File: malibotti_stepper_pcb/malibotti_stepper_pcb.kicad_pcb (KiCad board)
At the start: 2 copper layers, 80 x 65 mm, 40 parts, among them J1 Stepper 1, J5 USB_C_Receptacle_USB2.0_16P, J6 Conn_01x04, SW1 RST, SW8 BTN, U1 ESP32-C3-MINI-1, U2 XC6206PxxxMR, U3 STSPIN220

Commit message: Malibotti WIP
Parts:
- removed TP2: M1_1, TestPoint:TestPoint_Pad_1.5x1.5mm
- added C13: 1n, Capacitor_SMD:C_0402_1005Metric, B.Cu at (85.3, 105.7)
- added C14: 1n, Capacitor_SMD:C_0402_1005Metric, B.Cu at (85.5, 108.7)
- added C15: u1, Capacitor_SMD:C_0402_1005Metric, B.Cu at (89.3, 109.6)
- added C16: 22n, Capacitor_SMD:C_0402_1005Metric, B.Cu at (87.4, 110.5)
- added C17: 22u, Capacitor_SMD:C_0603_1608Metric, B.Cu at (92.0, 93.8)
- added C18: 2u2, Capacitor_SMD:C_0603_1608Metric, B.Cu at (92.0, 95.2)
- added J2: Stepper 1, liebler_CONN:JST_XH_5P_SMD, B.Cu at (100.2, 104.8)
- added J3: Servo, Connector_PinHeader_2.54mm:PinHeader_1x03_P2.54mm_Vertical, B.Cu at (134.4, 118.2)
- added J4: Conn_01x04, liebler_CONN:JST_XH_S4B-XH-A-1_1x04_P2.50mm_Horizontal_SmallerCourtyard, F.Cu at (104.8, 75.2)
- added R15: 1k, Resistor_SMD:R_0402_1005Metric, B.Cu at (85.3, 106.7)
- added R16: 1k, Resistor_SMD:R_0402_1005Metric, B.Cu at (84.5, 108.7)
- added R17: 1k, Resistor_SMD:R_0402_1005Metric, B.Cu at (90.2, 110.2)
- added R18: 1k, Resistor_SMD:R_0402_1005Metric, B.Cu at (87.4, 108.7)
- added R19: 10k, Resistor_SMD:R_0402_1005Metric, B.Cu at (86.5, 108.7)
- added R20: 1r0, Resistor_SMD:R_0805_2012Metric_Pad1.20x1.40mm_HandSolder, B.Cu at (92.0, 101.8)
- added R21: 1r0, Resistor_SMD:R_0805_2012Metric_Pad1.20x1.40mm_HandSolder, B.Cu at (92.0, 109.0)
- added R22: 10k, Resistor_SMD:R_0402_1005Metric, B.Cu at (95.3, 90.9)
- added R23: 10k, Resistor_SMD:R_0402_1005Metric, B.Cu at (88.3, 108.7)
- added R24: 5k1, Resistor_SMD:R_0402_1005Metric, B.Cu at (95.3, 89.0)
- added R25: 5k1, Resistor_SMD:R_0402_1005Metric, B.Cu at (88.3, 110.5)
- added R5: 1r0, Resistor_SMD:R_0805_2012Metric_Pad1.20x1.40mm_HandSolder, B.Cu at (92.0, 90.9)
- added R6: 1r0, Resistor_SMD:R_0805_2012Metric_Pad1.20x1.40mm_HandSolder, B.Cu at (92.0, 98.2)
- added U4: STSPIN220, Package_DFN_QFN:VQFN-16-1EP_3x3mm_P0.5mm_EP1.8x1.8mm, B.Cu at (88.5, 105.5)
- C7: footprint Capacitor_SMD:C_0603_1608Metric -> Capacitor_SMD:C_0402_1005Metric
- J1: footprint liebler_CONN:JST_XH_B5B-XH-A_1x05_P2.50mm_Vertical_smaller -> liebler_CONN:JST_XH_5P_SMD
- J6: moved to F.Cu
- R10: value 47k -> 10k
- U3: moved to B.Cu
- moved R9 129.2 mm to (90.7, 77.9), turned to -90 degrees
- moved R8 127.3 mm to (91.8, 77.9), turned to -90 degrees
- moved R1 125.7 mm to (89.8, 77.9), turned to -90 degrees
- moved R7 125.1 mm to (93.2, 77.8), turned to -90 degrees
- moved J6 123.5 mm to (117.5, 75.2)
- moved R4 118.4 mm to (102.3, 73.2), turned to 90 degrees
- moved R12 115.7 mm to (94.3, 89.8), turned to -90 degrees
- moved R3 115.3 mm to (104.8, 73.2), turned to 90 degrees
- moved R11 112.6 mm to (96.4, 90.9), turned to -90 degrees
- moved R14 112.3 mm to (99.2, 90.9), turned to 90 degrees
- moved R13 111.1 mm to (98.8, 92.8), turned to 0 degrees
- moved R10 111.0 mm to (97.3, 90.9), turned to -90 degrees
- moved C3 110.1 mm to (71.2, 115.4)
- moved C2 103.4 mm to (81.2, 90.6)
- moved SW8 102.2 mm to (83.5, 80.0), turned to -90 degrees
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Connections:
- J6 pad 2: BUZZER -> Net-(J6-Pin_2)
- R12 pad 1: PWM -> GND
- TP3 pad 1: /M1_2 -> unconnected-(TP3-Pad1)
- U1 pad 12: /M2_2 -> unconnected-(U1-GPIO0/ADC1_CH0/XTAL_32K_P-Pad12)
- U1 pad 13: /M2_1 -> unconnected-(U1-GPIO1/ADC1_CH1/XTAL_32K_N-Pad13)
- U1 pad 16: /M1_1 -> unconnected-(U1-GPIO10-Pad16)
- U1 pad 18: /M1_2 -> unconnected-(U1-GPIO4/ADC1_CH4-Pad18)
- U1 pad 30: BUZZER -> Net-(J6-Pin_2)
- U1 pad 5: SERVO2_ADC -> STEP2
- U1 pad 6: SERVO1_ADC -> DIR2
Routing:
- net /TX: track 0.00 -> 55.1 mm
- net Net-(J6-Pin_2): track 0.00 -> 52.3 mm
- net /USBD+: track 0.00 -> 47.9 mm
- net /USBD-: track 0.00 -> 47.1 mm
- net Net-(J2-Pin_2): track 0.00 -> 21.2 mm
- net Net-(J1-Pin_2): track 0.00 -> 21.1 mm
- net Net-(J1-Pin_1): track 0.00 -> 9.55 mm
- net Net-(J2-Pin_1): track 0.00 -> 7.46 mm
- net Net-(J1-Pin_3): track 0.00 -> 7.26 mm
- net Net-(J2-Pin_3): track 0.00 -> 7.23 mm
- net Net-(J1-Pin_4): track 0.00 -> 6.99 mm
- net Net-(J2-Pin_4): track 0.00 -> 6.94 mm
- net +3V3: track 0.00 -> 6.03 mm
- net Net-(J5-D--PadA7): track 0.00 -> 4.94 mm
- net Net-(U3-REF): track 0.00 -> 4.36 mm
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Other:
- board size 80 x 65 mm -> 70 x 65 mm

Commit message: WIP
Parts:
- J3: footprint Connector_PinHeader_2.54mm:PinHeader_1x03_P2.54mm_Vertical -> Connector_PinHeader_2.54mm:PinHeader_1x03_P2.54mm_Vertical_SMD_Pin1Left
- moved SW1 102.2 mm to (84.3, 120.8), turned to 90 degrees
- moved BZ1 65.7 mm to (101.1, 81.2), turned to 90 degrees
- moved J3 48.6 mm to (95.6, 88.9), turned to 90 degrees
- moved H1 44.0 mm to (120.5, 93.0)
- moved D21 35.0 mm to (79.8, 100.0), turned to -90 degrees
- moved C3 21.4 mm to (79.8, 95.8)
- moved R2 19.4 mm to (94.9, 84.5)
- moved C1 15.6 mm to (82.3, 73.3)
- moved C2 15.6 mm to (82.5, 75.0)
- moved U2 11.3 mm to (84.5, 77.5)
- moved C4 10.7 mm to (87.8, 78.5)
- moved SW8 6.38 mm to (87.4, 85.0), turned to 90 degrees
- moved C15 4.30 mm to (89.3, 113.9)
- moved J1 4.30 mm to (84.0, 99.2)
- moved J2 4.30 mm to (100.2, 109.2)
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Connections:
- net Net-(J6-Pin_2) renamed /RX
- C13 pad 1: RESET2 -> STEPPER_RESET
- C9 pad 1: RESET1 -> STEPPER_RESET
- R13 pad 1: RESET1 -> STEPPER_RESET
- R15 pad 1: RESET2 -> STEPPER_RESET
- R25 pad 1: +3V3 -> Net-(R23-Pad1)
- R25 pad 2: Net-(R23-Pad1) -> +3V3
- U1 pad 12: unconnected-(U1-GPIO0/ADC1_CH0/XTAL_32K_P-Pad12) -> BUZZER
- U1 pad 13: unconnected-(U1-GPIO1/ADC1_CH1/XTAL_32K_N-Pad13) -> STEPPER_RESET
- U1 pad 16: unconnected-(U1-GPIO10-Pad16) -> STEP1
- U1 pad 18: unconnected-(U1-GPIO4/ADC1_CH4-Pad18) -> DIR1
- U1 pad 19: SRV3 -> Servo1
- U3 pad 14: RESET1 -> STEPPER_RESET
- U4 pad 14: RESET2 -> STEPPER_RESET
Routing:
- net SCL: track 0.00 -> 50.8 mm, vias 0 -> 2
- net SDA: track 0.00 -> 50.0 mm, vias 0 -> 4
- net STEPPER_RESET: track 0.00 -> 46.5 mm, vias 0 -> 4
- net BUZZER: track 0.00 -> 46.4 mm, vias 0 -> 2
- net Servo1: track 0.00 -> 35.7 mm, vias 0 -> 2
- net RGB_LED: track 0.00 -> 32.4 mm, vias 0 -> 2
- net DIR1: track 0.00 -> 28.1 mm, vias 0 -> 2
- net STEP1: track 0.00 -> 25.6 mm, vias 0 -> 2
- net STEP2: track 0.00 -> 24.6 mm
- net DIR2: track 0.00 -> 21.0 mm
- net Net-(U1-EN/CHIP_PU): track 0.00 -> 7.11 mm
- net /USBD-: track 47.1 -> 53.4 mm
- net /USBD+: track 47.9 -> 54.2 mm
- net /RX: track 52.3 -> 56.0 mm
- net RESET1: track 2.33 -> 0.00 mm
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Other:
- board size 70 x 65 mm -> 70 x 68 mm

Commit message: WIP
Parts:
- moved C1 2.10 mm to (83.6, 75.0), turned to 180 degrees
- moved J5 1.80 mm to (90.2, 70.4)
- moved C2 1.60 mm to (83.3, 73.7)
- moved R1 1.55 mm to (88.9, 76.6)
- moved R8 1.36 mm to (91.4, 76.6)
- moved R3 1.35 mm to (104.9, 71.9)
- moved R4 1.35 mm to (102.3, 71.9)
- moved R9 1.33 mm to (90.4, 76.6)
- moved R2 1.31 mm to (95.8, 83.5), turned to -90 degrees
- moved R7 1.30 mm to (92.9, 76.6)
- moved C4 1.15 mm to (87.2, 77.5), turned to 0 degrees
- moved J4 1.15 mm to (104.8, 74.1)
- moved J6 1.15 mm to (117.5, 74.1)
- moved J2 1.12 mm to (100.8, 108.2)
- moved U2 0.34 mm to (84.3, 77.7)
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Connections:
- U1 pad 3: +3.3V -> +3V3
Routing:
- net +3V3: track 6.03 -> 133.0 mm, vias 0 -> 8
- net +5V: track 3.09 -> 112.1 mm, vias 0 -> 3
- net Net-(U1-GPIO9): track 0.00 -> 59.6 mm
- net GND: track 1.59 -> 21.3 mm, vias 0 -> 67
- net BUZZER: track 46.4 -> 55.8 mm
- net DIR1: track 28.1 -> 19.1 mm
- net RGB_LED: track 32.4 -> 40.8 mm
- net Net-(U1-EN/CHIP_PU): track 7.11 -> 14.3 mm, vias 0 -> 2
- net STEP1: track 25.6 -> 19.1 mm
- net Servo1: track 35.7 -> 31.1 mm
- net Net-(J2-Pin_1): track 7.46 -> 10.8 mm
- net DIR2: track 21.0 -> 23.7 mm
- net STEP2: track 24.6 -> 26.8 mm
- net STEPPER_RESET: track 46.5 -> 44.9 mm, vias 4 -> 2
- net Net-(J5-D+-PadA6): track 3.64 -> 5.03 mm
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- added copper zone on B.Cu, net GND
- added copper zone on F.Cu, net GND

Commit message: Malibotti Stepper Release Candidate
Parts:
- added G***: LOGO, LOGO, F.Cu at (71.4, 83.0)
- moved C2 27.0 mm to (110.1, 70.0), turned to 0 degrees
- moved C1 26.6 mm to (110.0, 71.3), turned to 0 degrees
- moved U2 24.2 mm to (107.9, 72.5), turned to 0 degrees
- moved C4 19.0 mm to (105.2, 71.7), turned to -90 degrees
- moved R16 1.19 mm to (85.0, 111.8), turned to 180 degrees
- moved R14 1.10 mm to (98.8, 96.2), turned to 0 degrees
- moved C13 0.75 mm to (85.8, 109.4), turned to 90 degrees
- moved R3 0.68 mm to (104.2, 71.7)
- moved C10 0.50 mm to (98.8, 95.2), turned to 0 degrees
- moved R15 0.36 mm to (85.0, 110.8)
- moved C14 0.30 mm to (85.5, 113.2)
- moved R4 0.25 mm to (102.5, 71.7)
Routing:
- net +3V3: track 133.0 -> 106.6 mm, vias 8 -> 4
- net Servo1: track 31.1 -> 35.7 mm, vias 2 -> 0
- net SDA: track 50.8 -> 52.6 mm
- net BUZZER: track 55.8 -> 54.1 mm
- net Net-(U1-EN/CHIP_PU): track 14.3 -> 12.7 mm
- net +5V: track 112.1 -> 110.5 mm
- net RGB_LED: track 40.8 -> 39.6 mm
- net GND: track 21.3 -> 20.2 mm, vias 67 -> 63
- net Net-(U1-GPIO9): track 59.6 -> 60.6 mm
- net Net-(U4-EN/FLT): track 3.54 -> 2.94 mm
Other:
- board text added: "2026-04-08 k.liebler@hs-osnabrueck.de"
- board text added: "3V3"
- board text added: "5V"
- board text added: "BTN"
- board text added: "G"
- board text added: "GND"
- board text added: "INFO"
- board text added: "MaliBotti"
- board text added: "RST"
- board text added: "RX"
- board text added: "SCL"
- board text added: "SDA"
- board text added: "Stepper 1"
- board text added: "Stepper 2"
- board text added: "TX"
- board text added: "USB-C"

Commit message: Limit Switch
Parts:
- added SW2: MicroSwitchLeft, liebler_MECH:Omron D2F Left Angled, F.Cu at (64.0, 95.9)
- added SW3: MicroSwitchRight, liebler_MECH:Omron D2F Right Angled, F.Cu at (64.1, 104.1)
- moved G*** 19.3 mm to (88.0, 92.8)
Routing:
- net BUZZER: track 54.1 -> 70.1 mm, vias 2 -> 4
- net GND: track 20.2 -> 22.9 mm
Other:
- outline, holes or cut-outs redrawn

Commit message: Minor improvements
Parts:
- moved G*** 10.2 mm to (88.2, 82.7)
- moved SW3 0.16 mm to (64.0, 104.0)
- moved SW2 0.12 mm to (64.0, 96.0)

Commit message: update to Kicad 10
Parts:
- moved C3 0.30 mm to (79.8, 95.5)
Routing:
- net GND: track 22.6 -> 27.4 mm, vias 63 -> 134
- net +5V: track 110.5 -> 109.1 mm
- net BUZZER: track 70.0 -> 69.4 mm

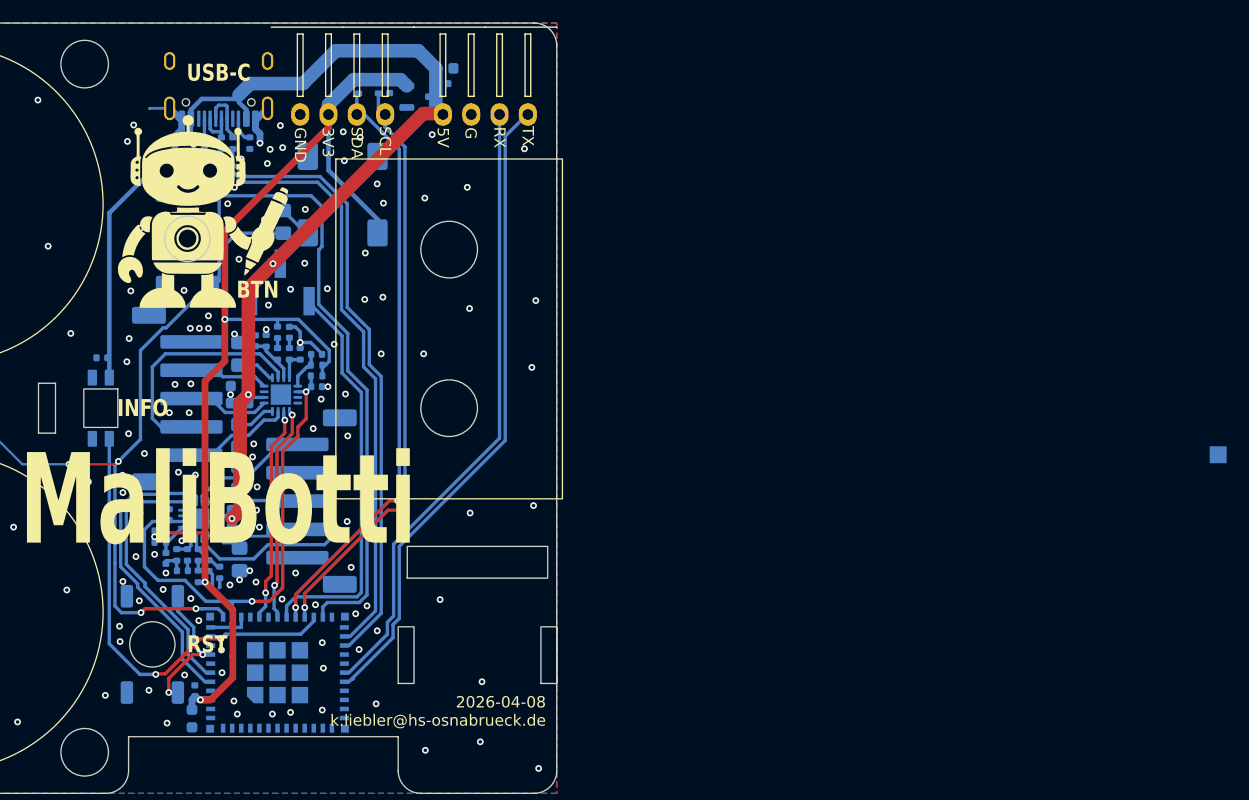
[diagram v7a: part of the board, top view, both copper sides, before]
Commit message: Malibotti stepper as ordered @ JLCPCB
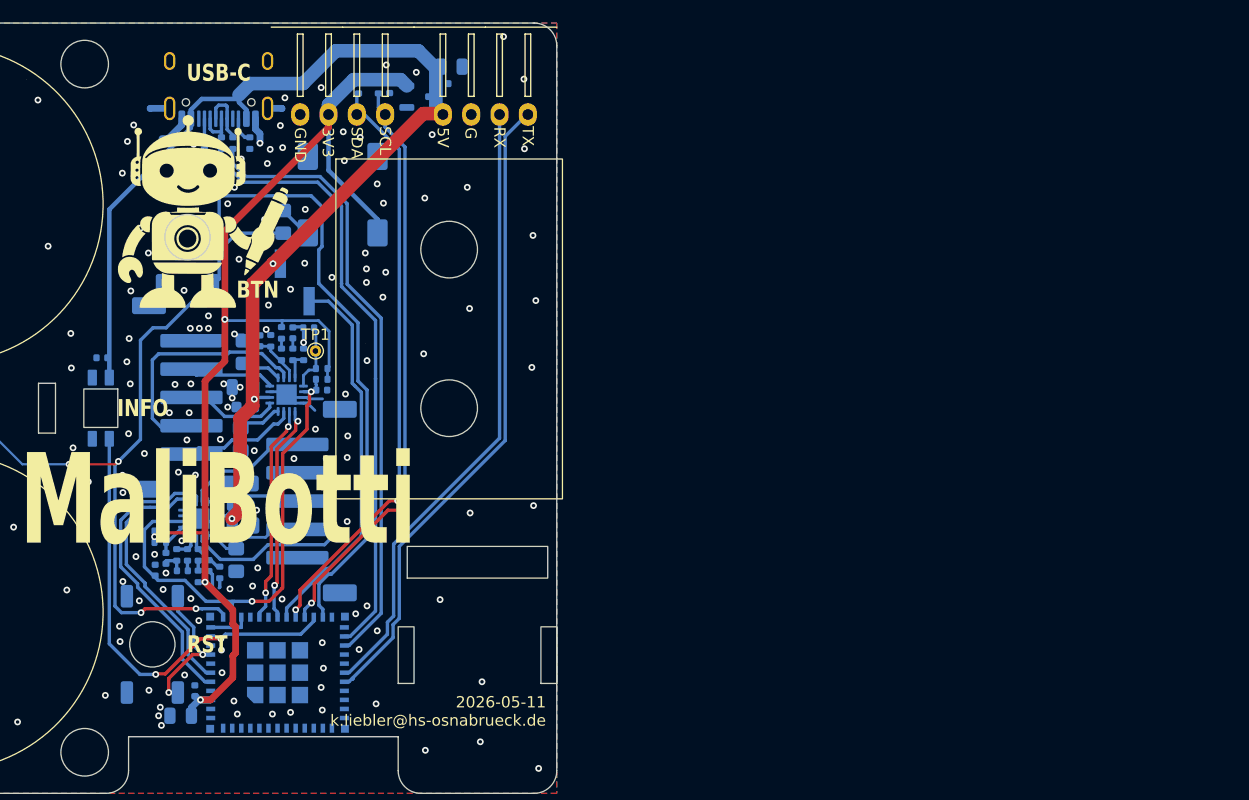
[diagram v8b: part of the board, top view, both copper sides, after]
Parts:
- removed TP3: M1_2, TestPoint:TestPoint_Pad_1.5x1.5mm
- added TP1: TestPoint, TestPoint:TestPoint_THTPad_D1.0mm_Drill0.5mm, F.Cu at (98.7, 95.0)
- C12, C17, C2, C5: footprint Capacitor_SMD:C_0603_1608Metric -> Capacitor_SMD:C_0805_2012Metric
- moved C13 5.06 mm to (84.5, 114.3)
- moved C10 2.45 mm to (98.1, 92.9), turned to 180 degrees
- moved C12 1.03 mm to (86.8, 127.2), turned to 180 degrees
- moved C2 0.62 mm to (110.7, 69.8)
- moved C18 0.61 mm to (92.5, 99.9)
- moved C9 0.54 mm to (99.2, 98.4)
- moved R13 0.54 mm to (99.2, 97.5)
- moved R14 0.54 mm to (99.2, 96.5)
- moved R20 0.52 mm to (92.1, 106.7), turned to 0 degrees
- moved U3 0.50 mm to (96.2, 98.8)
- moved R5 0.43 mm to (92.3, 95.0)
- moved C6 0.40 mm to (92.1, 108.6)
- moved R12 0.40 mm to (94.8, 94.0)
- moved C8 0.40 mm to (93.8, 94.0)
- moved R22 0.35 mm to (95.7, 95.2)
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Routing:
- net GND: track 27.4 -> 32.4 mm, vias 134 -> 152
- net Net-(U3-EN/FLT): track 3.40 -> 5.96 mm
- net +3V3: track 107.1 -> 109.6 mm
- net Servo1: track 35.7 -> 33.7 mm
- net +5V: track 109.1 -> 110.2 mm
- net Net-(U1-GPIO9): track 60.6 -> 59.5 mm
- net Net-(J1-Pin_3): track 7.26 -> 8.32 mm
- net Net-(J1-Pin_2): track 21.1 -> 22.1 mm
- net Net-(J1-Pin_4): track 6.99 -> 7.67 mm
- net STEP2: track 26.8 -> 26.1 mm
- net Net-(J2-Pin_3): track 7.54 -> 8.09 mm
- net BUZZER: track 69.4 -> 69.9 mm
- net STEPPER_RESET: track 45.2 -> 45.7 mm
- net Net-(J1-Pin_1): track 9.55 -> 10.1 mm
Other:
- board text added: "2026-05-11 k.liebler@hs-osnabrueck.de"
- board text removed: "2026-04-08 k.liebler@hs-osnabrueck.de"
